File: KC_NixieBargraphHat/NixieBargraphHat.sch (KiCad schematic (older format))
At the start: 50 parts, among them J1 Screw_Terminal_1x03, J2 Screw_Terminal_1x02, J3 Screw_Terminal_1x03, J4 Screw_Terminal_1x03, Q1 FDD7N25LZTM, Q2 2N7002, Q3 FDD7N25LZTM, Q4 2N7002, U1 MCP6411, U2 Raspberry_PI_Zero_Header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

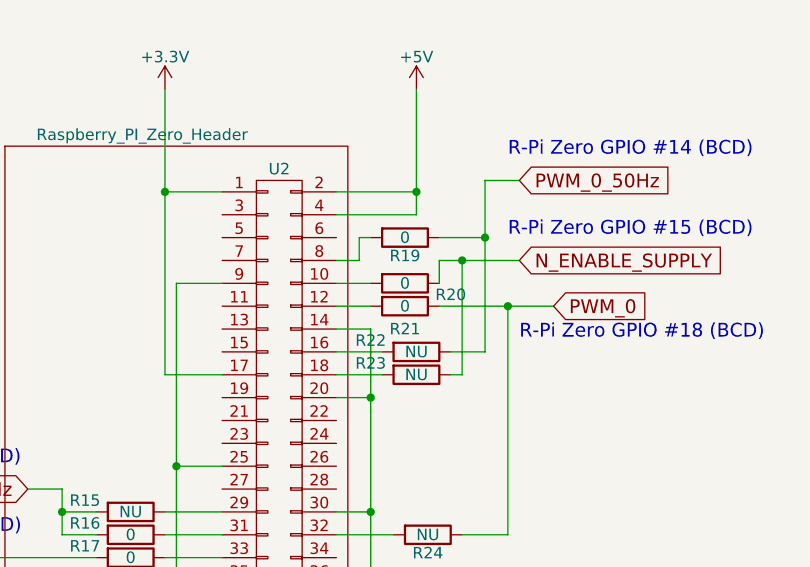
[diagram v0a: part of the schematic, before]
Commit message: update BOM to add 1k to enable pin
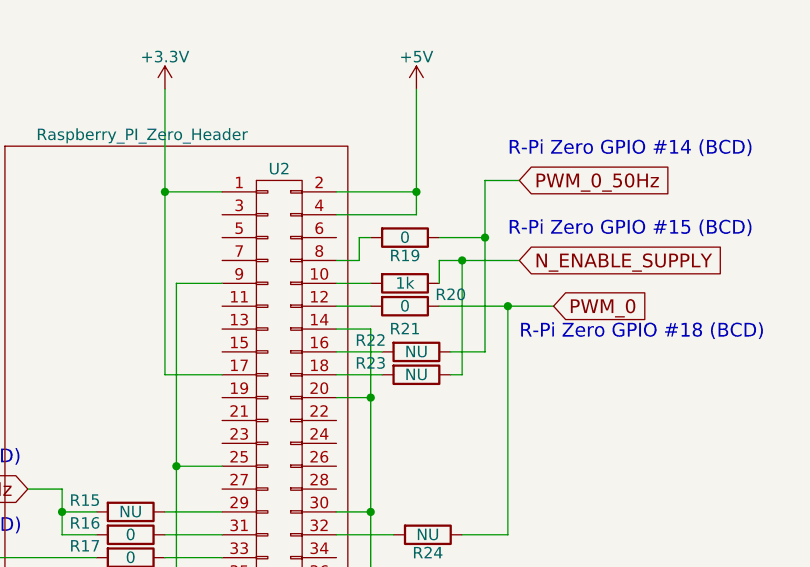
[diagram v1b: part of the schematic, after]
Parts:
- R20: value 0 -> 1k
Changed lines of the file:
@@
 P 9400 4350
 F 0 "R20" V 9450 4550 50  0000 C CNN
-F 1 "0" V 9400 4350 50  0000 C CNN
+F 1 "1k" V 9400 4350 50  0000 C CNN
 F 2 "Resistors_SMD:R_0805_HandSoldering" V 9330 4350 50  0001 C CNN
-F 3 "" H 9400 4350 50  0001 C CNN
+F 3 "https://www.digikey.com/product-detail/en/yageo/RC0805FR-071KL/311-1.00KCRCT-ND/730391" H 9400 4350 50  0001 C CNN
 	1    9400 4350
 	0    1    1    0

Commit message: updated the schematic
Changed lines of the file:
@@
 $EndComp
 Wire Wire Line
-	5650 2650 5650 3200
+	5650 2650 5650 3050
+Wire Wire Line
+	5650 3050 5650 3200
 Wire Wire Line
 	5650 3500 5650 3600
 Wire Wire Line
-	4350 2650 4800 2650
-Wire Wire Line
-	2350 2100 3600 2100
+	4350 2650 4450 2650
+Wire Wire Line
+	4450 2650 4800 2650
+Wire Wire Line
+	2350 2100 2500 2100
+Wire Wire Line
+	2500 2100 3250 2100
+Wire Wire Line
+	3250 2100 3600 2100
 Wire Wire Line
 	3600 2100 3600 2550
@@
 	3600 2550 3750 2550
 Wire Wire Line
-	3600 2750 3750 2750
+	3600 2750 3700 2750
+Wire Wire Line
+	3700 2750 3750 2750
 Connection ~ 5650 3050
 Wire Wire Line
@@
 	5650 950  5650 1050
 Wire Wire Line
-	5650 2100 5650 2250
-Wire Wire Line
-	5650 1350 5650 1500
+	5650 2100 5650 2150
+Wire Wire Line
+	5650 2150 5650 2250
+Wire Wire Line
+	5650 1350 5650 1450
+Wire Wire Line
+	5650 1450 5650 1500
 Wire Wire Line
 	2500 2200 2500 2100
 Connection ~ 2500 2100
 Wire Wire Line
-	2950 1300 2950 2400
+	2950 1300 2950 1350
+Wire Wire Line
+	2950 1350 2950 1800
+Wire Wire Line
+	2950 1800 2950 2400
 Wire Wire Line
 	3150 2700 3250 2700
@@
 	2950 3100 2950 3000
 Wire Wire Line
-	3950 1300 3950 2350
+	3950 1300 3950 1900
+Wire Wire Line
+	3950 1900 3950 2350
 Wire Wire Line
 	5200 2650 5100 2650
@@
 	8850 2150 9400 2150
 Wire Wire Line
-	9400 2000 9400 2350
+	9400 2000 9400 2150
+Wire Wire Line
+	9400 2150 9400 2350
 Wire Wire Line
 	9400 2350 8850 2350
@@
 Wire Wire Line
 	9050 1050 9050 1000
-Text GLabel 9900 4250 2    60   Input ~ 0
+Text GLabel 10300 4250 2    60   Input ~ 0
 N_ENABLE_SUPPLY
 Text Notes 9850 4150 0    60   ~ 0
@@
 	9550 4350 9550 4250
 Wire Wire Line
-	9550 4250 9900 4250
+	9550 4250 9650 4250
+Wire Wire Line
+	9650 4250 10300 4250
 Text Notes 9900 4600 0    60   ~ 0
 R-Pi Zero GPIO #18 (BCD)
@@
 	9100 4850 9250 4850
 Wire Wire Line
-	9250 4550 9250 6000
+	9250 4550 9250 4850
+Wire Wire Line
+	9250 4850 9250 5350
+Wire Wire Line
+	9250 5350 9250 6000
 Wire Wire Line
 	9100 5350 9250 5350
@@
 	8400 5850 8600 5850
 Wire Wire Line
-	8400 4350 8400 6000
+	8400 4350 8400 5150
+Wire Wire Line
+	8400 5150 8400 5850
+Wire Wire Line
+	8400 5850 8400 6000
 Wire Wire Line
 	8600 5150 8400 5150
@@
 	9450 4050 9100 4050
 Wire Wire Line
-	9450 3500 9450 4050
+	9450 3500 9450 3950
+Wire Wire Line
+	9450 3950 9450 4050
 Wire Wire Line
 	9100 3950 9450 3950
@@
 	8600 3950 8350 3950
 Wire Wire Line
-	8350 3500 8350 4750
+	8350 3500 8350 3950
+Wire Wire Line
+	8350 3950 8350 4750
 Wire Wire Line
 	8350 4750 8600 4750
@@
 PWM_0_50Hz
 Wire Wire Line
-	3950 1900 4600 1900
+	3950 1900 4300 1900
+Wire Wire Line
+	4300 1900 4600 1900
 $Comp
 L +5V #PWR016
@@
 $EndComp
 Wire Wire Line
-	6000 6000 6000 6550
+	6000 6000 6000 6400
+Wire Wire Line
+	6000 6400 6000 6550
 Wire Wire Line
 	6000 6850 6000 6950
 Wire Wire Line
-	4700 6000 5150 6000
-Wire Wire Line
-	2700 5450 3950 5450
+	4700 6000 4800 6000
+Wire Wire Line
+	4800 6000 5150 6000
+Wire Wire Line
+	2700 5450 2850 5450
+Wire Wire Line
+	2850 5450 3600 5450
+Wire Wire Line
+	3600 5450 3950 5450
 Wire Wire Line
 	3950 5450 3950 5900
@@
 	3950 5900 4100 5900
 Wire Wire Line
-	3950 6100 4100 6100
+	3950 6100 4050 6100
+Wire Wire Line
+	4050 6100 4100 6100
 Wire Wire Line
 	4050 6100 4050 6400
@@
 	6000 4300 6000 4400
 Wire Wire Line
-	6000 5450 6000 5600
-Wire Wire Line
-	6000 4700 6000 4850
+	6000 5450 6000 5500
+Wire Wire Line
+	6000 5500 6000 5600
+Wire Wire Line
+	6000 4700 6000 4800
+Wire Wire Line
+	6000 4800 6000 4850
 Wire Wire Line
 	2850 5550 2850 5450
 Connection ~ 2850 5450
 Wire Wire Line
-	3300 4650 3300 5750
+	3300 4650 3300 5250
+Wire Wire Line
+	3300 5250 3300 5750
 Wire Wire Line
 	3500 6050 3600 6050
@@
 	3300 6450 3300 6350
 Wire Wire Line
-	4300 4650 4300 5700
+	4300 4650 4300 5250
+Wire Wire Line
+	4300 5250 4300 5700
 Wire Wire Line
 	5550 6000 5450 6000
@@
 R-Pi Zero GPIO #6 (BCD)
 Wire Wire Line
-	4300 5250 4950 5250
+	4300 5250 4650 5250
+Wire Wire Line
+	4650 5250 4950 5250
 $Comp
 L +5V #PWR025
@@
 Connection ~ 4300 5250
 Wire Wire Line
-	9750 3900 9750 4650
+	9750 3900 9750 4150
+Wire Wire Line
+	9750 4150 9750 4650
 Wire Wire Line
 	9750 3900 9900 3900
@@
 PWM_1_50Hz
 Wire Wire Line
-	7900 5250 7900 5450
+	7900 5250 7900 5350
+Wire Wire Line
+	7900 5350 7900 5450
 Wire Wire Line
 	7900 5250 7750 5250
@@
 	5450 6400 6000 6400
 Wire Wire Line
-	4050 6400 5150 6400
+	4050 6400 4800 6400
+Wire Wire Line
+	4800 6400 5150 6400
 $Comp
 L R R8
@@
 Connection ~ 3700 2750
 Wire Wire Line
-	3700 3050 4800 3050
+	3700 3050 4450 3050
+Wire Wire Line
+	4450 3050 4800 3050
 $Comp
 L D_x2_Serial_AKC D4
@@
 $EndComp
 Wire Wire Line
-	6950 5550 8050 5550
+	6950 5550 7300 5550
+Wire Wire Line
+	7300 5550 8050 5550
 Wire Wire Line
 	8350 5550 8600 5550
@@
 $EndComp
 Wire Wire Line
-	9550 4450 10050 4450
+	9550 4450 9850 4450
+Wire Wire Line
+	9850 4450 10050 4450
 $Comp
 L R R24
